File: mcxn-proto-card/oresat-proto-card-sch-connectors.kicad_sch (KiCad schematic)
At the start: 13 parts, among them J1 J-SAMTEC-TFM-110-01-L-D-RA, J2 U.FL, J3 U.FL, J4 U.FL, J6 J-SAMTEC-TFM-120-X1-XXX-D-RA

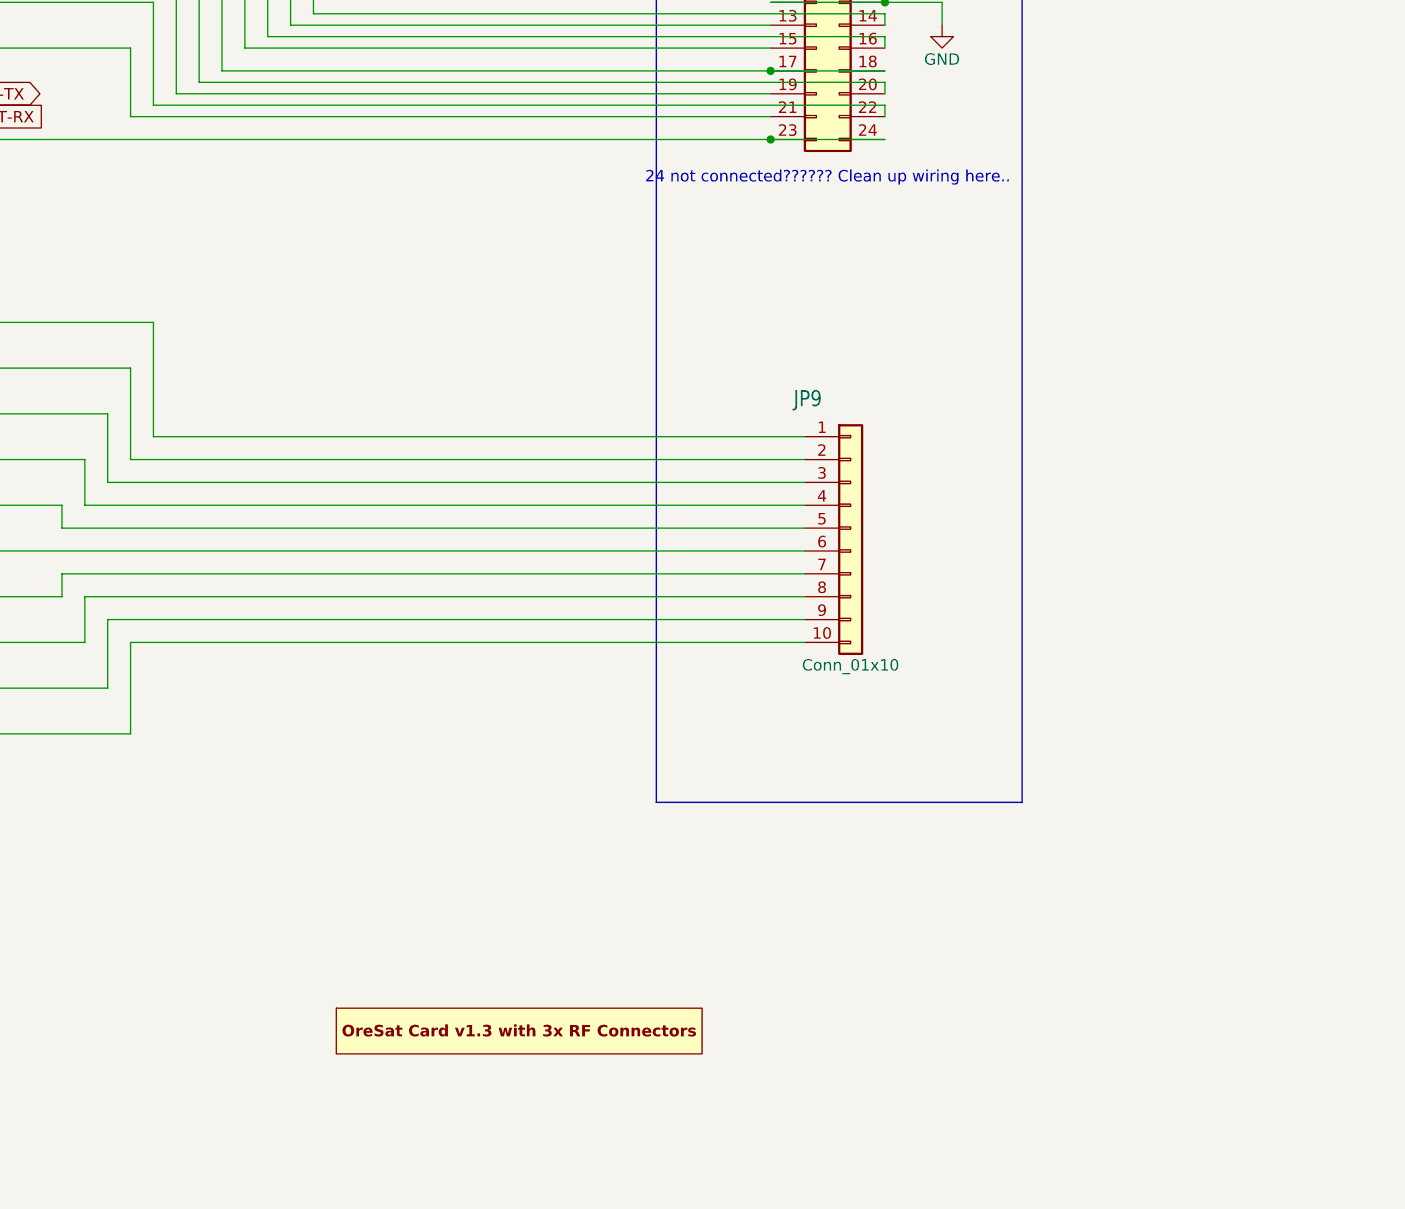
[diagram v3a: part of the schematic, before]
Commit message: Eagle libraries removed and replaced, schematic and layout clean up
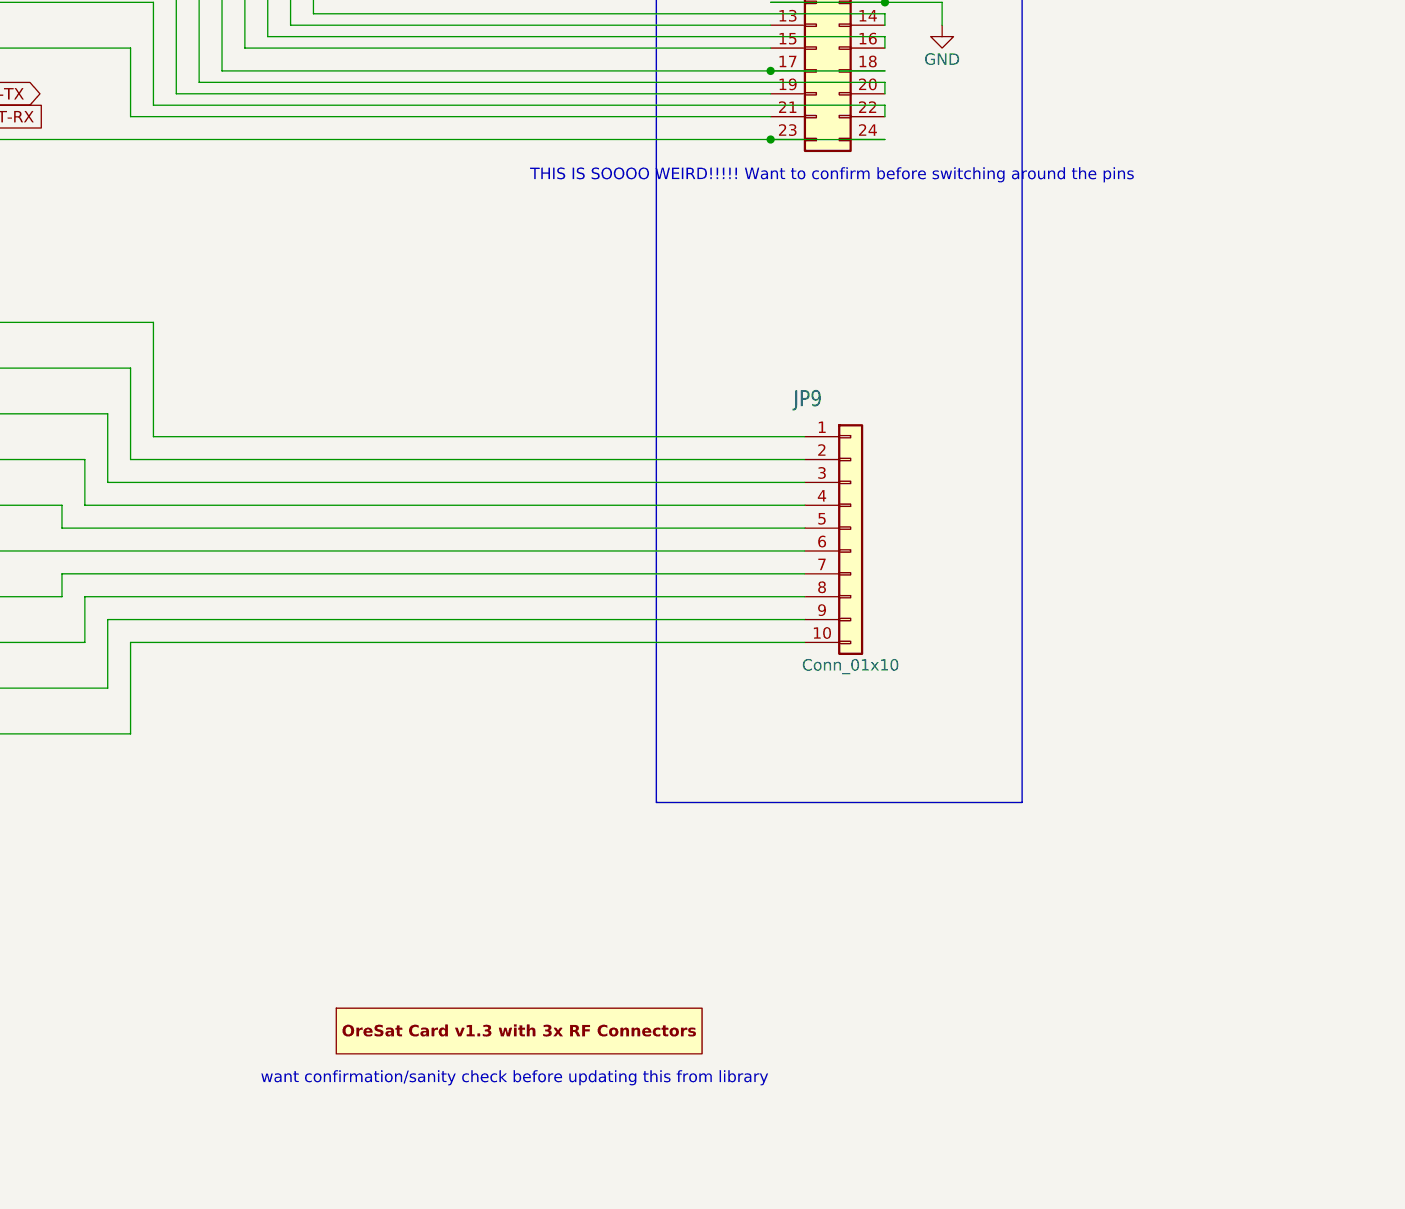
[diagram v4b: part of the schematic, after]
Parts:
- JP9: footprint oresat-proto-card:1X10 -> Connector_PinHeader_2.54mm:PinHeader_1x10_P2.54mm_Vertical
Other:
- note added: "THIS IS SOOOO WEIRD!!!!! Want to confirm before switching around the pins"
- note added: "want confirmation/sanity check before updating this from library"
- note removed: "24 not connected?????? Clean up wiring here.."
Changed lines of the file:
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@@
 		)
 	)
+	(text "want confirmation/sanity check before updating this from library"
+		(exclude_from_sim no)
+		(at 162.052 249.174 0)
+		(effects
+			(font
+				(size 1.27 1.27)
+			)
+		)
+	)
 	(text "OreSat Power Domain signals\n(See power sheet)"
 		(exclude_from_sim no)
@@
 		)
 	)
-	(text "24 not connected?????? Clean up wiring here.."
+	(text "THIS IS SOOOO WEIRD!!!!! Want to confirm before switching around the pins"
 		(exclude_from_sim no)
-		(at 196.85 149.098 0)
+		(at 197.358 148.844 0)
 		(effects
 			(font
@@
 			)
 		)
-		(property "Footprint" "oresat-proto-card:1X10"
+		(property "Footprint" "Connector_PinHeader_2.54mm:PinHeader_1x10_P2.54mm_Vertical"
 			(at 199.39 187.96 0)
 			(effects

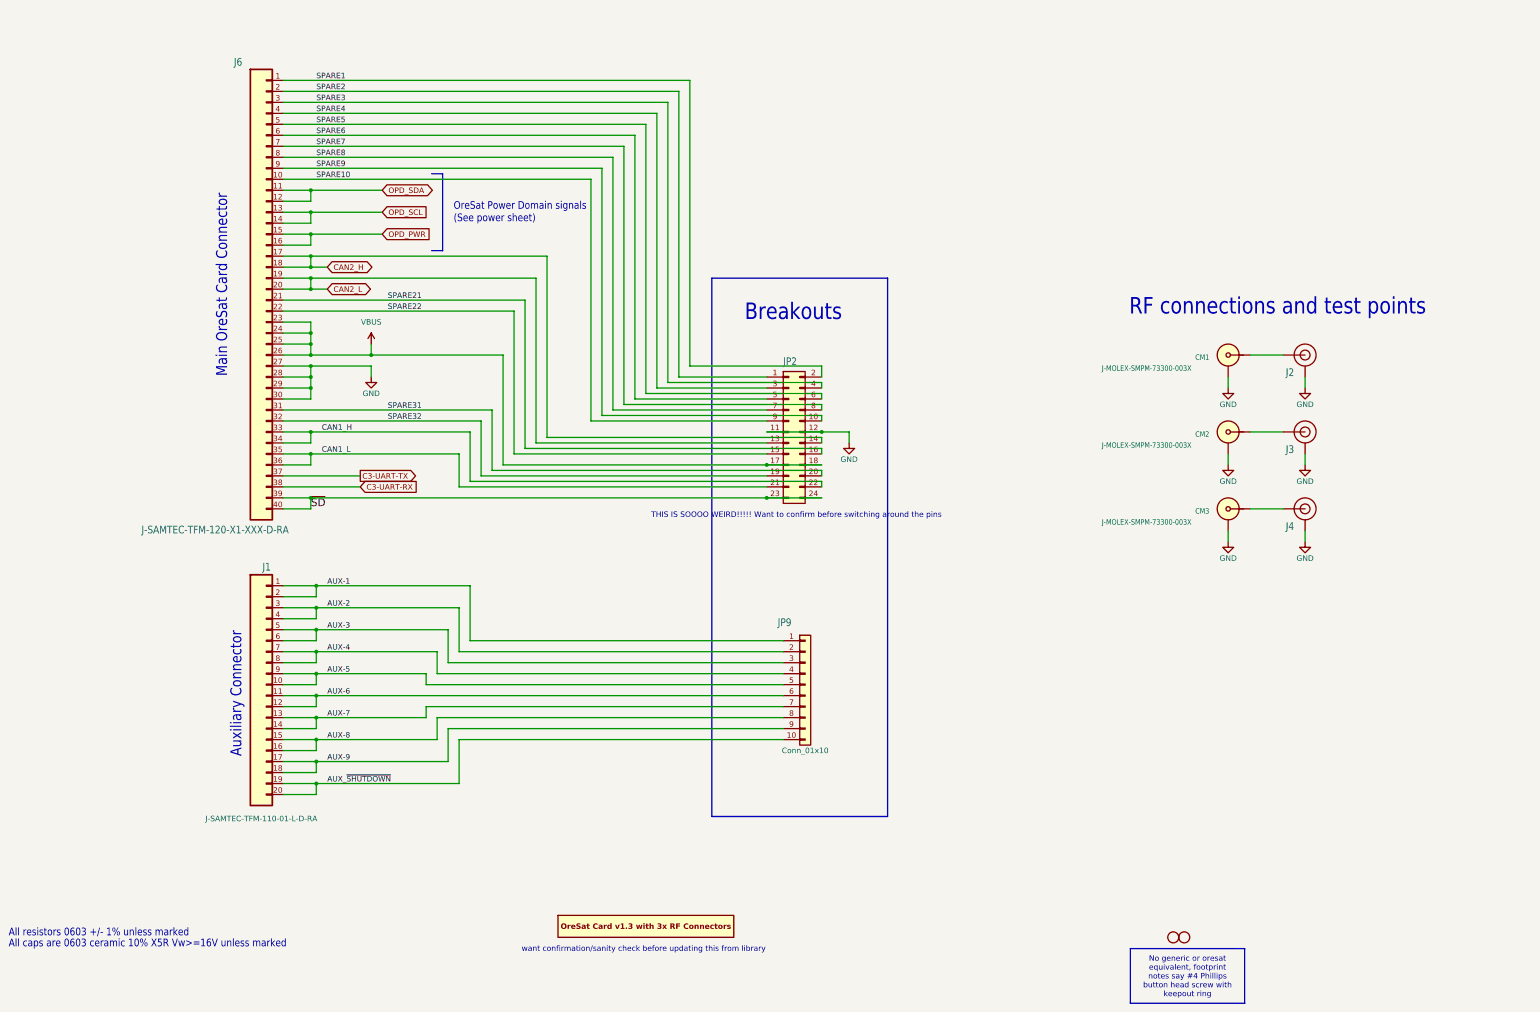
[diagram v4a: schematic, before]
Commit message: Eagle libraries replaced, scheatic and layout clean up cont.
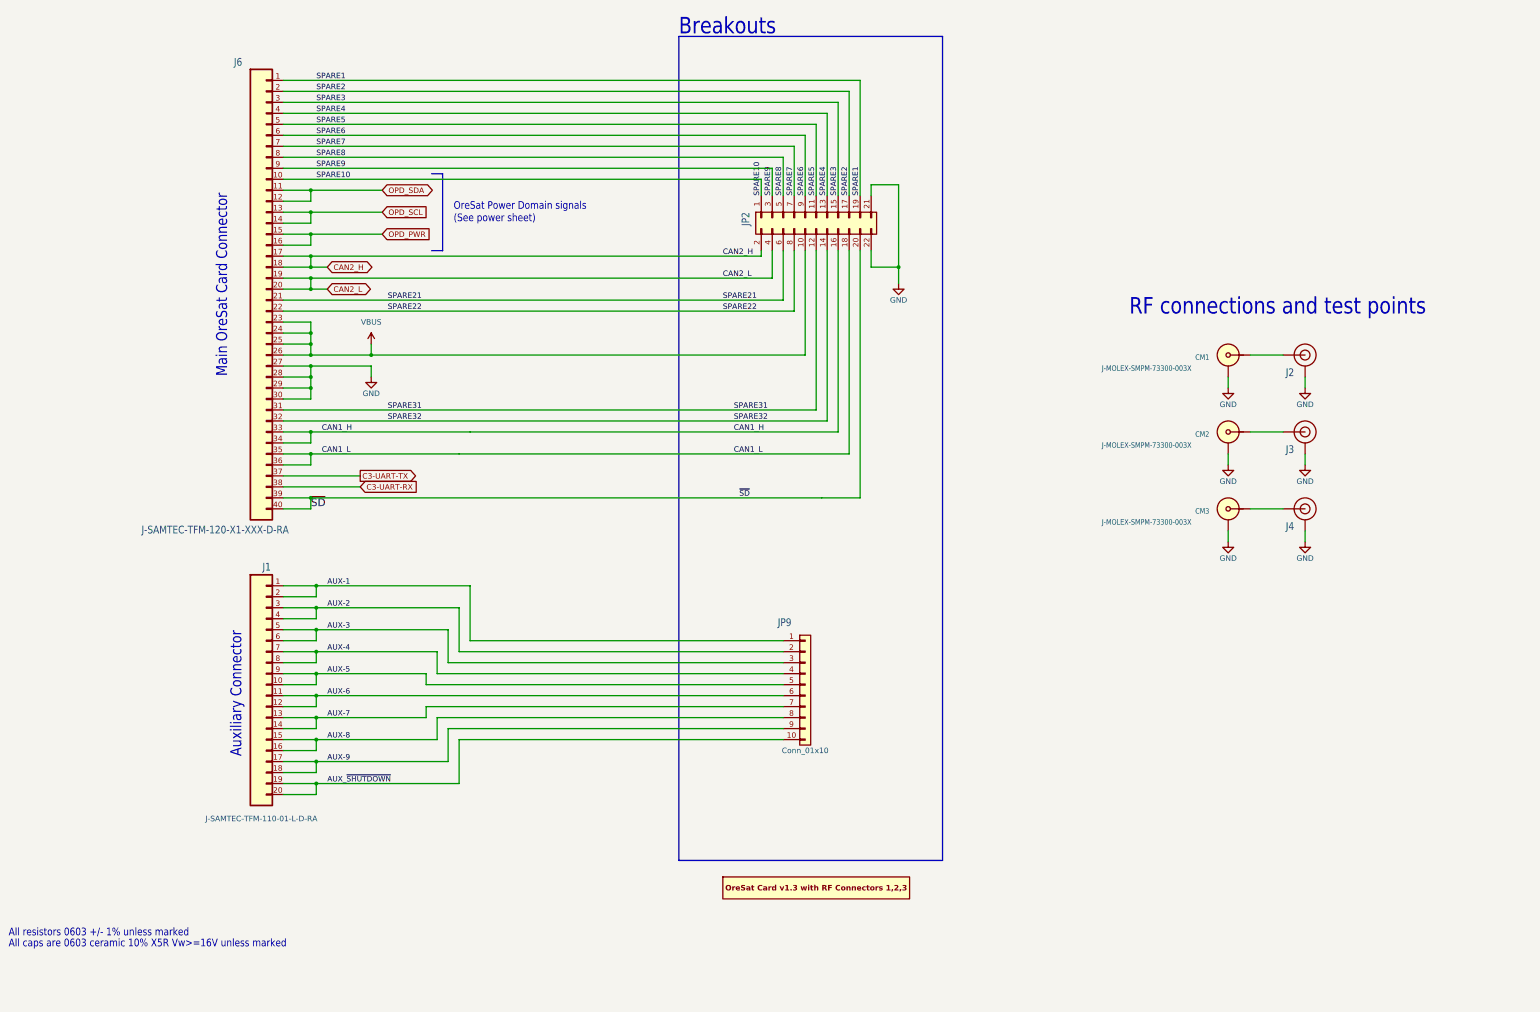
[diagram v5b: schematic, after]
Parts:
- removed H2, H3: STAND-OFFTIGHT, oresat-proto-card:STAND-OFF-TIGHT, symbol oresat-proto-card-eagle-import:STAND-OFFTIGHT
- JP2: symbol Connector_Generic:Conn_02x12_Odd_Even -> Connector_Generic:Conn_02x11_Odd_Even
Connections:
- net CAN1_H: now also JP2.16 (Pin_16); no longer JP2.22 (Pin_22)
- net CAN1_L: now also JP2.18 (Pin_18); no longer JP2.21 (Pin_21)
- net CAN2_H: now also JP2.2 (Pin_2); no longer JP2.14 (Pin_14)
- net CAN2_L: now also JP2.4 (Pin_4); no longer JP2.13 (Pin_13)
- net GND: now also JP2.21 (Pin_21), JP2.22 (Pin_22); no longer JP2.11 (Pin_11), JP2.12 (Pin_12)
- net SPARE1: now also JP2.19 (Pin_19); no longer JP2.2 (Pin_2)
- net SPARE10: now also JP2.1 (Pin_1); no longer JP2.9 (Pin_9)
- net SPARE2: now also JP2.17 (Pin_17); no longer JP2.1 (Pin_1)
- net SPARE21: now also JP2.6 (Pin_6); no longer JP2.16 (Pin_16)
- net SPARE22: now also JP2.8 (Pin_8); no longer JP2.15 (Pin_15)
- net SPARE3: now also JP2.15 (Pin_15); no longer JP2.4 (Pin_4)
- net SPARE31: now also JP2.12 (Pin_12); no longer JP2.20 (Pin_20)
- net SPARE32: now also JP2.14 (Pin_14); no longer JP2.19 (Pin_19)
- net SPARE4: now also JP2.13 (Pin_13); no longer JP2.3 (Pin_3)
- net SPARE5: now also JP2.11 (Pin_11); no longer JP2.6 (Pin_6)
- net SPARE6: now also JP2.9 (Pin_9); no longer JP2.5 (Pin_5)
- net SPARE7: now also JP2.7 (Pin_7); no longer JP2.8 (Pin_8)
- net SPARE8: now also JP2.5 (Pin_5); no longer JP2.7 (Pin_7)
- net SPARE9: now also JP2.3 (Pin_3); no longer JP2.10 (Pin_10)
- net VBUS: now also JP2.10 (Pin_10); no longer JP2.17 (Pin_17), JP2.18 (Pin_18)
- net ~{SD}: now also JP2.20 (Pin_20); no longer JP2.23 (Pin_23), JP2.24 (Pin_24)
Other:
- note removed: "THIS IS SOOOO WEIRD!!!!! Want to confirm before switching around the pins"
- note removed: "want confirmation/sanity check before updating this from library"
